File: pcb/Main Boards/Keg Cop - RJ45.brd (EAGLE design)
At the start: 45 x 51 mm, 9 parts, among them X2 RJ45-8X

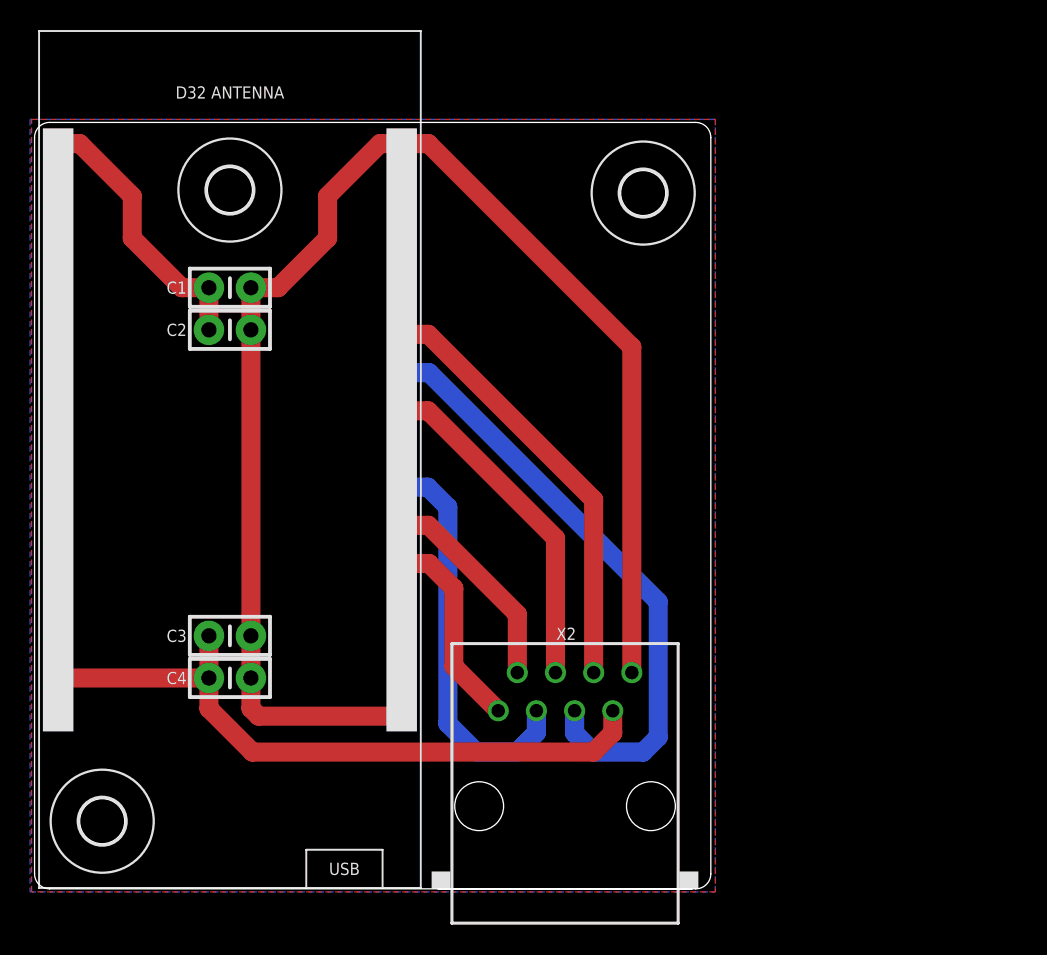
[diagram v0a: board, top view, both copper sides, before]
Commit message: Swap pins, split dirs
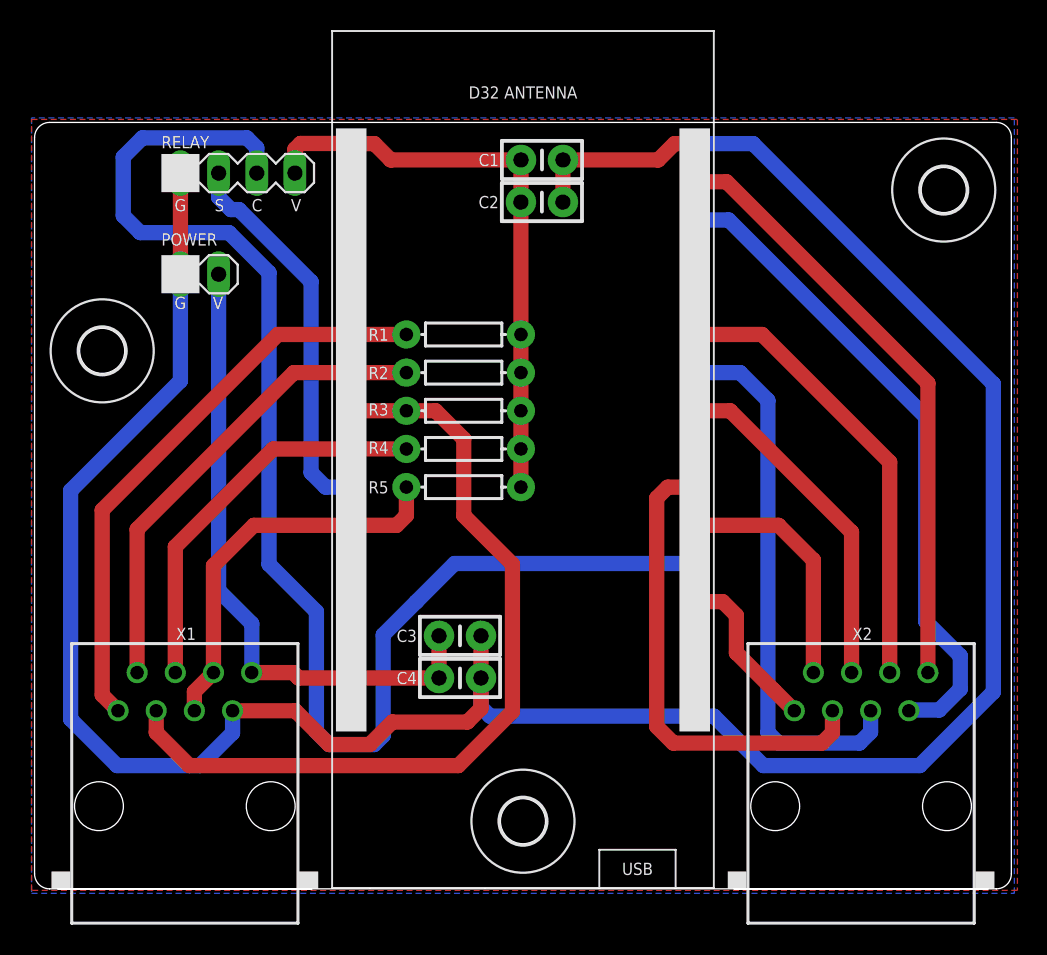
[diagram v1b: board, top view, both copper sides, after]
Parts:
- added POWER: 2-PIN, Donnie:HDR-2_VERT
- added R1, R2, R3, R4, R5: 2.2kΩ, SparkFun-Resistors:AXIAL-0.3
- added RELAY: 4-PIN, Donnie:MA04-1
- added X1: RJ45-8X, con-tycoelectronics:RJ45-NO-SHIELD
- moved U$2 46.3 mm to (32.5, 4.50)
- moved U$1 31.3 mm to (4.50, 35.8)
- moved C1 22.4 mm to (33.8, 48.5)
- moved C2 22.4 mm to (33.8, 45.7)
- moved U$3 20.0 mm to (60.5, 46.5)
- moved X2 19.7 mm to (55.0, 5.50)
- moved D32 19.5 mm to (32.5, 29.3)
- moved C3 15.3 mm to (28.3, 16.8)
- moved C4 15.3 mm to (28.3, 14.0)
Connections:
- removed net VCC: C1.1, C2.1, D32.VCC
- new net 3V3: C1.1, C2.1, D32.VCC, R1.P$1, R2.P$1, R3.P$1, R4.P$1, R5.P$1, RELAY.4
- new net COOL: D32.IO4, RELAY.3
- new net KDAT: D32.IO14, R5.P$2, X1.5, X1.6
- new net KEG7: D32.IO22, X2.7
- new net KEG8: D32.IO23, X2.8
- new net LDAT: D32.IO26, R4.P$2, X1.4
- new net RDAT: D32.IO32, R1.P$2, X1.1
- new net SOL: D32.IO27, RELAY.2
- new net TDAT: D32.IO33, R2.P$2, X1.2
- new net UDAT: D32.IO25, R3.P$2, X1.3
- net 5V: now also POWER.2, X1.8; no longer X2.7
- net GND: now also POWER.1, RELAY.1, X1.7; no longer X2.8
- net KEG1: now also D32.IO0; no longer D32.IO4
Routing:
- net COOL: track 0.00 -> 92.8 mm
- net GND: track 96.5 -> 175.8 mm
- net UDAT: track 0.00 -> 55.3 mm
- net KEG7: track 0.00 -> 43.9 mm
- net KEG8: track 0.00 -> 40.3 mm
- net 3V3: track 0.00 -> 39.2 mm
- net RDAT: track 0.00 -> 38.9 mm
- net TDAT: track 0.00 -> 31.8 mm
- net LDAT: track 0.00 -> 26.6 mm
- net KDAT: track 0.00 -> 26.3 mm
- net SOL: track 0.00 -> 25.9 mm
- net VCC: track 18.4 -> 0.00 mm
- net KEG3: track 26.7 -> 31.9 mm
- net KEG5: track 40.4 -> 36.6 mm
- net KEG1: track 13.5 -> 11.1 mm
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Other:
- board size 45 x 51 mm -> 65 x 51 mm
- board text added: "5 - KDAT 6 - DNC 7 - GND 8 - 5V"
- board text added: "C"
- board text added: "G"
- board text added: "S"
- board text added: "V"
- board text added: "X1 1 - RDAT 2 - TDAT 3 - UDAT 4 - LDAT"
- board text added: "X2 1 - KEG1 2 - KEG2 3 - KEG3 4 - KEG4"
- board text removed: "1 - KEG1 2 - KEG2 3 - KEG3 4 - KEG4"

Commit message: Renamed files
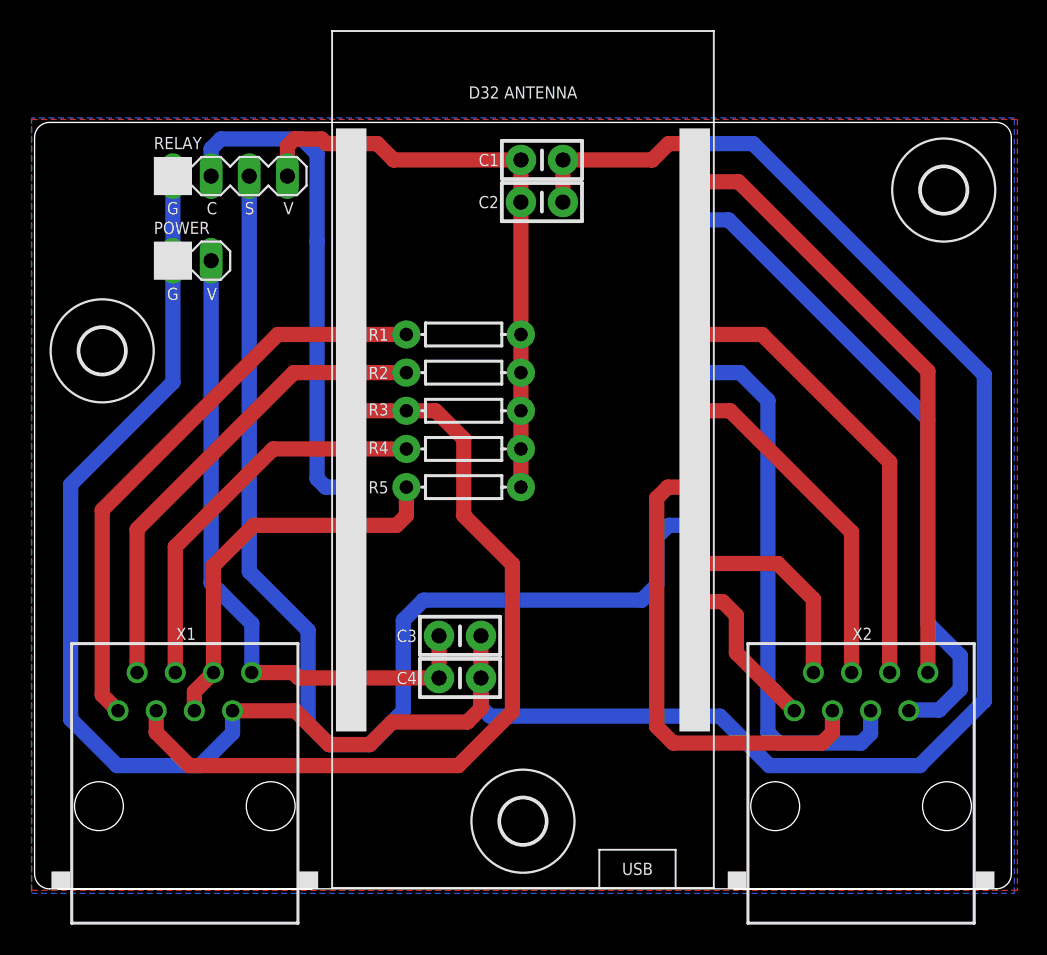
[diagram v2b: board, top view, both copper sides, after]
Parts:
- moved POWER 1.03 mm to (9.21, 41.8)
- moved RELAY 0.54 mm to (13.0, 47.4)
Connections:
- net COOL: now also D32.IO27, RELAY.2; no longer D32.IO4, RELAY.3
- net KEG2: now also D32.IO4; no longer D32.IO16
- net SOL: now also D32.IO16, RELAY.3; no longer D32.IO27, RELAY.2
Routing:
- net COOL: track 92.8 -> 33.7 mm
- net SOL: track 25.9 -> 75.8 mm
- net KEG2: track 16.3 -> 13.8 mm
- net 5V: track 42.9 -> 44.0 mm
- net GND: track 175.8 -> 174.9 mm
- net 3V3: track 39.2 -> 40.1 mm
